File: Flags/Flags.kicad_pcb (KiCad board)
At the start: 2 copper layers, 63.5 x 41.9 mm, 22 parts, among them J1 Conn_01x07_Male, J2 Conn_01x06_Male, J3 Conn_01x04_Male, J4 Conn_01x03_Male, U1 74HC74, U2 74LS08, U3 74LS175

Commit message: Polishing Flags
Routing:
- net /CF: track 24.2 -> 19.9 mm
- net /~ZF: track 58.6 -> 55.4 mm
- net Net-(U1-Pad11): track 42.1 -> 40.2 mm
- net /C2: track 51.3 -> 49.6 mm
- net /ZF: track 25.9 -> 25.7 mm, vias 0 -> 2
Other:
- board text added: "+5V"
- board text added: "08"
- board text added: "174"
- board text added: "175"
- board text added: "24.02.2023"
- board text added: "74HCPU"
- board text added: "C2"
- board text added: "CMP"
- board text added: "EQ ="
- board text added: "Enable"
- board text added: "Flags"
- board text added: "GT >"
- board text added: "Gnd"
- board text added: "INPUTS"
- board text added: "LT <"
- board text added: "OUTPUT"
- board text added: "Vcc"
- board text added: "~RES"

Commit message: Polishing Flags
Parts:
- renumbered D3 to D2, D7 to D3, D8 to D4, D9 to D5, J4 to J3, J3 to J4, R5 to R2, R7 to R4, R10 to R5, R11 to R6, R12 to R7, U2 to U1, U1 to U2

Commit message: Lost origin
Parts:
- moved J4 62.7 mm to (78.7, 48.3)
- moved C3 62.7 mm to (28.3, 32.4)
- moved J3 62.7 mm to (20.3, 55.9)
- moved U1 62.7 mm to (43.2, 33.0)
- moved C1 62.7 mm to (67.9, 34.9)
- moved C2 62.7 mm to (46.7, 34.3)
- moved D1 62.7 mm to (63.5, 26.0)
- moved D3 62.7 mm to (21.6, 26.0)
- moved J1 62.7 mm to (40.6, 55.9)
- moved J2 62.7 mm to (53.3, 21.6)
- moved R1 62.7 mm to (63.5, 29.8)
- moved R2 62.7 mm to (63.5, 20.0)
- moved R3 62.7 mm to (74.3, 33.7)
- moved R5 62.7 mm to (21.6, 20.0)
- moved U2 62.7 mm to (63.5, 33.0)
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
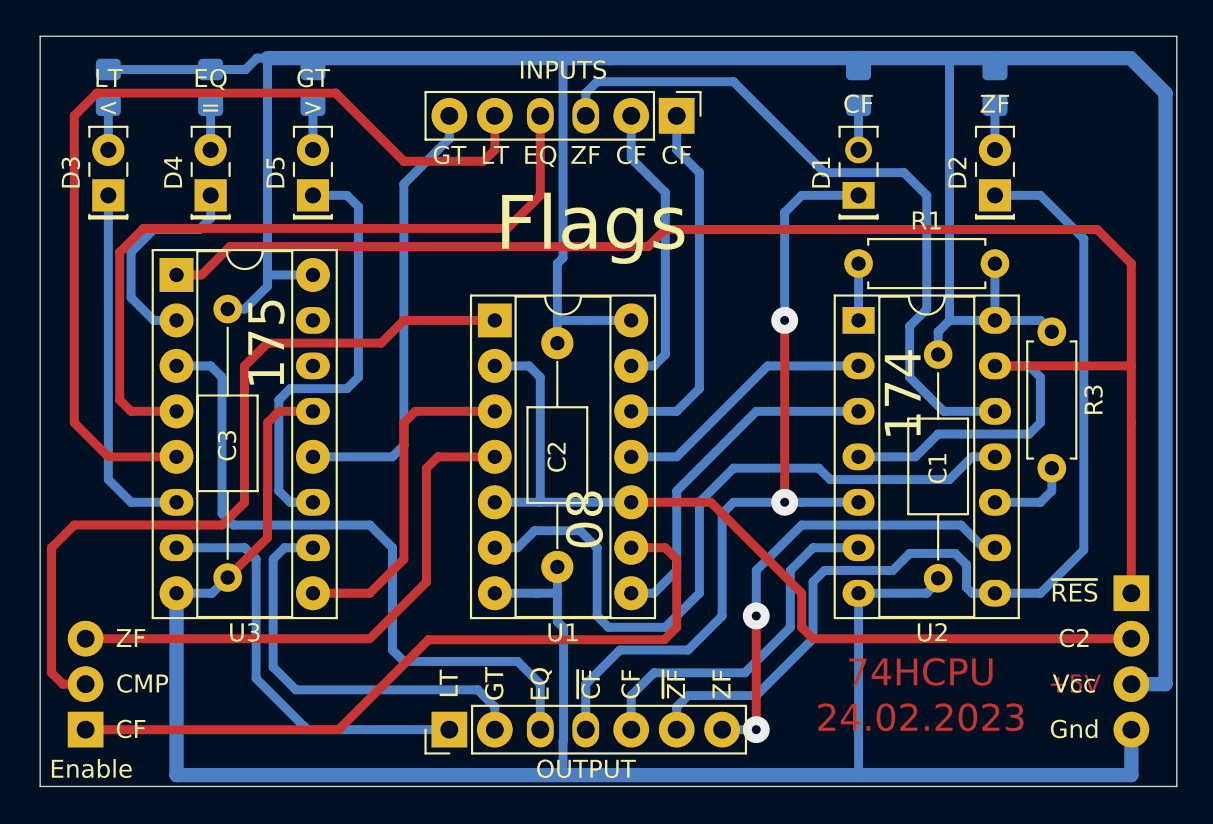
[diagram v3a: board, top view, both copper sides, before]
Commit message: Polishing Flags. Add lost pins.
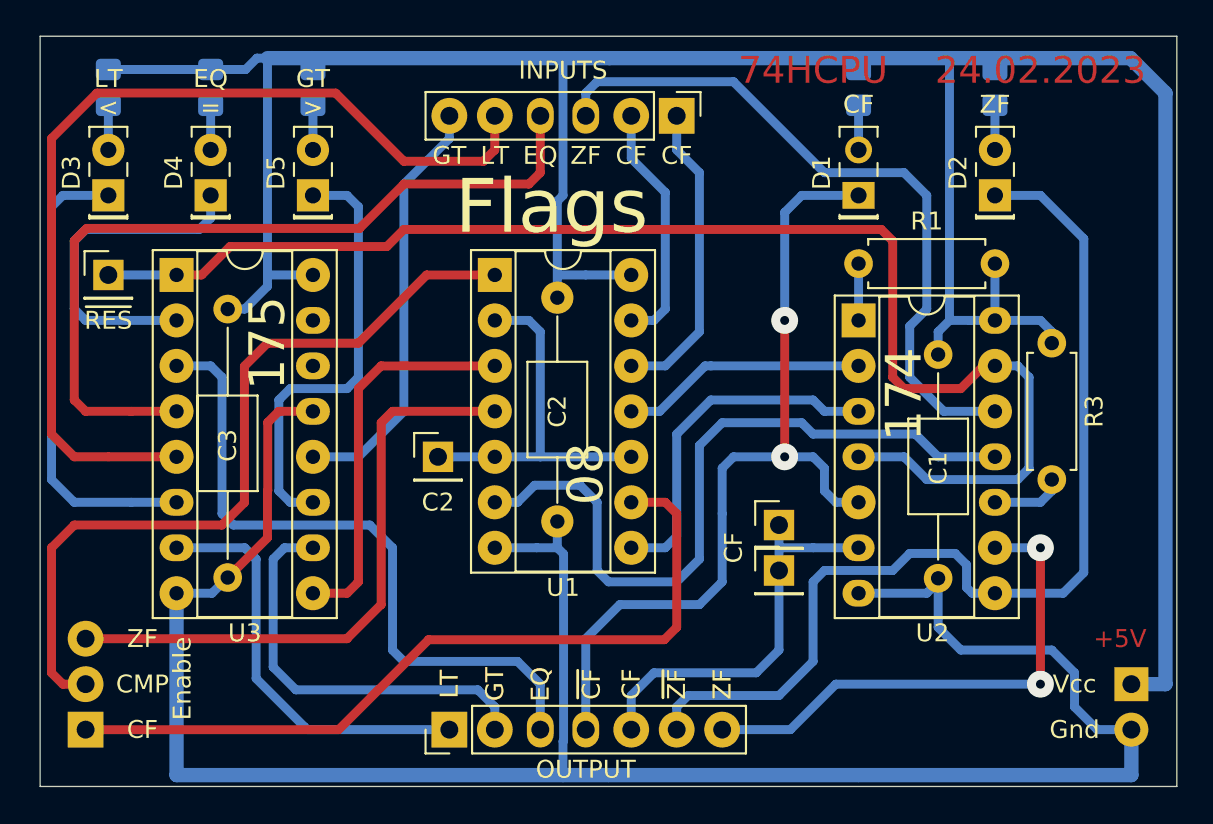
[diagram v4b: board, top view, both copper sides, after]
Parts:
- added J5: Conn_01x01_Male, Connector_PinHeader_2.54mm:PinHeader_1x01_P2.54mm_Vertical, F.Cu at (59.1, 44.5)
- added J6: Conn_01x01_Male, Connector_PinHeader_2.54mm:PinHeader_1x01_P2.54mm_Vertical, F.Cu at (59.1, 47.0)
- added J7: Conn_01x01_Male, Connector_PinHeader_2.54mm:PinHeader_1x01_P2.54mm_Vertical, F.Cu at (40.0, 40.6)
- added J8: Conn_01x02_Male, Connector_PinHeader_2.54mm:PinHeader_1x02_P2.54mm_Vertical, B.Cu at (78.7, 53.3)
- J4: value Conn_01x04_Male -> Conn_01x01_Male; footprint Connector_PinHeader_2.54mm:PinHeader_1x04_P2.54mm_Vertical -> Connector_PinHeader_2.54mm:PinHeader_1x01_P2.54mm_Vertical; moved to F.Cu
- moved J4 59.9 mm to (21.6, 30.5), turned to 0 degrees
- moved U1 2.54 mm to (43.2, 30.5)
- moved C2 2.54 mm to (46.7, 31.8)
- moved R3 0.63 mm to (74.3, 34.3)
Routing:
- net /C2: track 49.6 -> 20.6 mm
- net /~RES_FL: track 97.5 -> 76.8 mm
- net GND: track 112.0 -> 121.4 mm
- net /~EQ: track 12.1 -> 19.2 mm
- net /~LT: track 20.2 -> 26.2 mm
- net /~EQ_IN: track 40.9 -> 45.7 mm
- net /ZF_EN: track 30.8 -> 34.1 mm
- net /ZF: track 25.7 -> 29.0 mm
- net /~CF1_IN: track 20.1 -> 17.2 mm
- net Net-(U1-Pad3): track 18.8 -> 21.7 mm
- net /CF: track 19.9 -> 22.6 mm
- net /~CF2_IN: track 16.3 -> 13.8 mm
- net /CF_EN: track 42.0 -> 44.5 mm
- net /~CF: track 46.1 -> 48.2 mm
- net /LT_IN: track 51.4 -> 53.6 mm
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
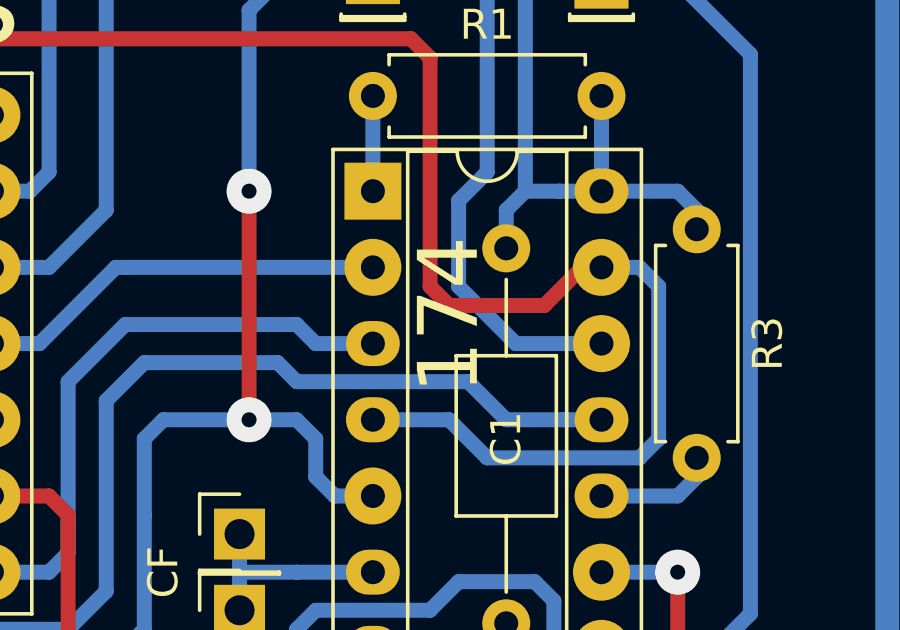
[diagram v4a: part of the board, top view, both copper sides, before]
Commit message: Fix mistype on silk
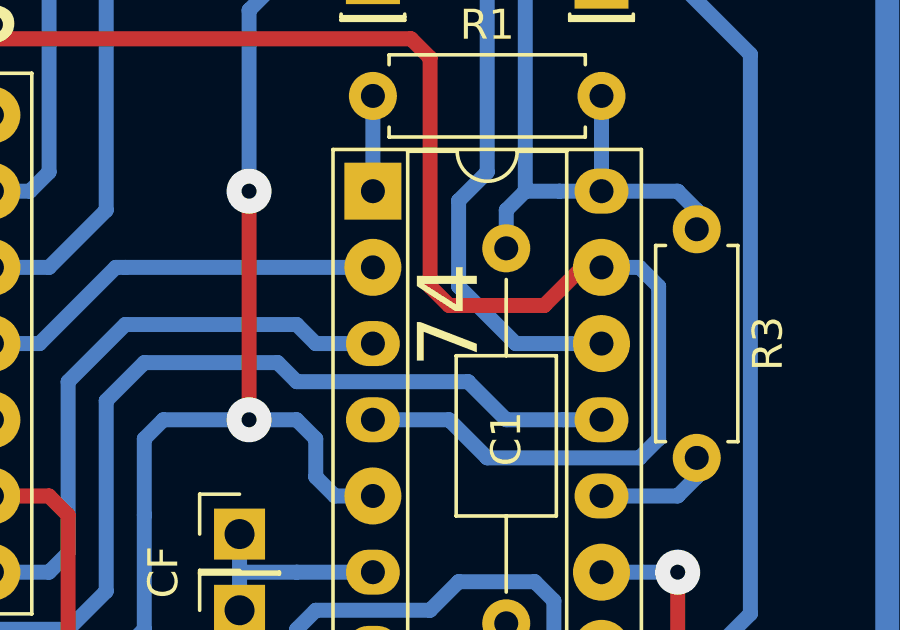
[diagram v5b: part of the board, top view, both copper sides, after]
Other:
- board text added: "74"
- board text removed: "174"

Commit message: Polishing Flags. Add mounting holes.
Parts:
- added H1: MountingHole, MountingHole:MountingHole_3.2mm_M3, F.Cu at (77.5, 21.6)
- added H2: MountingHole, MountingHole:MountingHole_3.2mm_M3, F.Cu at (26.0, 55.2)
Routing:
- net /~RES_FL: track 76.8 -> 83.2 mm, vias 0 -> 1
- net GND: track 121.4 -> 116.2 mm
- net /LT_IN: track 53.6 -> 55.8 mm
- net /CF_EN: track 44.5 -> 45.7 mm
- net /GT: track 23.1 -> 22.0 mm
- net /LT: track 23.4 -> 22.4 mm
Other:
- board size 63.5 x 41.9 mm -> 63.5 x 41.6 mm
- board text added: "20.05.2023"
- board text added: "OUTPUTS"
- board text removed: "24.02.2023"
- board text removed: "OUTPUT"

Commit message: Polishing Flags
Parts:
- added H3: MountingHole, MountingHole:MountingHole_3.2mm_M3, F.Cu at (21.6, 21.3)
- added H4: MountingHole, MountingHole:MountingHole_3.2mm_M3, F.Cu at (77.5, 55.2)
- J3, J8: moved to F.Cu
- moved D3 6.35 mm to (27.9, 26.0)
- moved J3 6.35 mm to (20.3, 49.5), turned to 180 degrees
- moved J8 6.35 mm to (78.7, 47.0), turned to 0 degrees
- moved R5 6.35 mm to (27.9, 20.0)
- moved D4 4.45 mm to (31.8, 26.0)
- moved H2 4.45 mm to (21.6, 55.2)
- moved R6 4.45 mm to (31.8, 20.0)
- moved D5 2.54 mm to (35.6, 26.0)
- moved R7 2.54 mm to (35.6, 20.0)
- moved H1 0.32 mm to (77.5, 21.3)
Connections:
- J3 pad 2: /CMP_EN -> /ZF_EN
- J3 pad 3: /ZF_EN -> /CMP_EN
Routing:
- net VCC: track 159.9 -> 142.0 mm
- net /CMP_EN: track 44.7 -> 33.1 mm
- net GND: track 116.2 -> 108.0 mm
- net /~LT: track 26.2 -> 30.7 mm
- net /LT_IN: track 55.8 -> 52.2 mm
- net /CF_EN: track 45.7 -> 43.5 mm
- net /ZF: track 29.0 -> 27.1 mm
- net /ZF_EN: track 34.1 -> 35.9 mm
- net /~EQ: track 19.2 -> 20.9 mm
- net /~GT: track 24.5 -> 23.4 mm
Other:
- board text added: "21.05.2023"
- board text removed: "20.05.2023"

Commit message: Polishing Flags
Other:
- board text added: "~EQ"
